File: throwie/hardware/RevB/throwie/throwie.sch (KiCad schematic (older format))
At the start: 24 parts, among them J1 CONN, Q1 2SC3356, Q2 SS8050-G, T1 TestPoints, T2 TestPoints, T3 TestPoints, T4 TestPoints, U1 C8051F850-A-GU, U2 MIC5231-3.3YM5-TR, X1 RO3101

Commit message: more layout
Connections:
- net 0.471: now also U1.2 (P0.2); no longer U1.14 (P1.4)
- net GNDREF: now also X1.3
- net at C4.2, Q1.1, Q2.3: no longer X1.3
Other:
- moved on the sheet: C4, Q2, R1
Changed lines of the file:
@@
 L throwie:RES_0603 R1
 U 1 1 6159CB9B
-P 5900 4650
-F 0 "R1" H 6075 4460 50  0000 C CNN
-F 1 "RES_0603" V 6075 4738 50  0001 L CNN
-F 2 "throwie:0603" H 5900 4650 50  0001 C CNN
-F 3 "" H 5900 4650 50  0001 C CNN
-F 4 "18K" H 6075 4551 50  0000 C CNN "Resistance"
-	1    5900 4650
+P 5950 4850
+F 0 "R1" H 6125 4660 50  0000 C CNN
+F 1 "RES_0603" V 6125 4938 50  0001 L CNN
+F 2 "throwie:0603" H 5950 4850 50  0001 C CNN
+F 3 "" H 5950 4850 50  0001 C CNN
+F 4 "18K" H 6125 4751 50  0000 C CNN "Resistance"
+	1    5950 4850
 	-1   0    0    1
 $EndComp
@@
 L power:GNDREF #PWR0111
 U 1 1 6159EFA4
-P 6250 4950
-F 0 "#PWR0111" H 6250 4700 50  0001 C CNN
-F 1 "GNDREF" H 6255 4777 50  0000 C CNN
-F 2 "" H 6250 4950 50  0001 C CNN
-F 3 "" H 6250 4950 50  0001 C CNN
-	1    6250 4950
+P 6250 5100
+F 0 "#PWR0111" H 6250 4850 50  0001 C CNN
+F 1 "GNDREF" H 6255 4927 50  0000 C CNN
+F 2 "" H 6250 5100 50  0001 C CNN
+F 3 "" H 6250 5100 50  0001 C CNN
+	1    6250 5100
 	1    0    0    -1
 $EndComp
@@
 L throwie:SS8050-G Q2
 U 1 1 615A6F3E
-P 6150 4650
-F 0 "Q2" H 6294 4696 50  0000 L CNN
-F 1 "SS8050-G" H 6294 4605 50  0000 L CNN
-F 2 "throwie:SS8050-G" H 6150 4650 50  0001 C CNN
-F 3 "" H 6150 4650 50  0001 C CNN
-	1    6150 4650
+P 6150 4850
+F 0 "Q2" H 6294 4896 50  0000 L CNN
+F 1 "SS8050-G" H 6294 4805 50  0000 L CNN
+F 2 "throwie:SS8050-G" H 6150 4850 50  0001 C CNN
+F 3 "" H 6150 4850 50  0001 C CNN
+	1    6150 4850
 	1    0    0    -1
 $EndComp
@@
 L throwie:CAP_0603 C4
 U 1 1 615A7727
-P 7000 4050
-F 0 "C4" H 7098 3971 50  0000 L CNN
-F 1 "CAP_0603" H 7098 3925 50  0001 L CNN
-F 2 "throwie:0603" H 7000 4050 50  0001 C CNN
-F 3 "" H 7000 4050 50  0001 C CNN
-F 4 "15pF" H 7098 3880 50  0000 L CNN "Capacitance"
-	1    7000 4050
+P 7100 4300
+F 0 "C4" H 7198 4221 50  0000 L CNN
+F 1 "CAP_0603" H 7198 4175 50  0001 L CNN
+F 2 "throwie:0603" H 7100 4300 50  0001 C CNN
+F 3 "" H 7100 4300 50  0001 C CNN
+F 4 "15pF" H 7198 4130 50  0000 L CNN "Capacitance"
+	1    7100 4300
 	1    0    0    -1
 $EndComp
@@
 $EndComp
 $Comp
-L throwie:RO3101 X1
-U 1 1 615AFB47
-P 6800 3950
-F 0 "X1" H 6800 4175 50  0000 C CNN
-F 1 "RO3101" H 6800 4084 50  0000 C CNN
-F 2 "throwie:R03101" H 6800 3950 50  0001 C CNN
-F 3 "" H 6800 3950 50  0001 C CNN
-	1    6800 3950
-	1    0    0    -1
-$EndComp
-$Comp
 L throwie:433MHz A1
 U 1 1 615B7977
@@
 	6600 3150 6600 3050
 Wire Wire Line
-	6250 4150 6250 4350
-Wire Wire Line
-	6250 4350 6800 4350
-Wire Wire Line
-	7000 4350 7000 4300
-Connection ~ 6250 4350
-Wire Wire Line
-	6250 4350 6250 4450
-Wire Wire Line
-	6800 4100 6800 4350
-Connection ~ 6800 4350
-Wire Wire Line
-	6800 4350 7000 4350
-Wire Wire Line
 	6650 3950 6600 3950
 Connection ~ 6600 3950
 Wire Wire Line
-	6950 3950 7000 3950
-Wire Wire Line
-	7000 3950 7000 4050
-Wire Wire Line
-	7000 3950 7000 3050
-Wire Wire Line
 	6250 3050 6600 3050
-Connection ~ 7000 3950
 Connection ~ 6600 3050
-Wire Wire Line
-	6600 3050 7000 3050
-Wire Wire Line
-	5550 4650 5200 4650
 Text Label 1200 3800 0    50   ~ 0
 MOD
-Text Label 1200 4400 0    50   ~ 0
+Text Label 1250 3300 0    50   ~ 0
 0.471
-Text Label 5200 4650 0    50   ~ 0
+Text Label 5200 4850 0    50   ~ 0
 MOD
 Wire Wire Line
@@
 	1050 1800 1050 1750
 Wire Wire Line
-	5900 4650 6050 4650
-Wire Wire Line
-	6250 4950 6250 4850
-Wire Wire Line
-	1800 4400 1200 4400
-NoConn ~ 1800 3300
-Wire Wire Line
 	1800 3800 1200 3800
-NoConn ~ 1800 3400
 $Comp
 L throwie:CAP_0603 C6
@@
 Wire Wire Line
 	5550 1400 5550 1350
+$Comp
+L throwie:RO3101 X1
+U 1 1 615AFB47
+P 6800 3950
+F 0 "X1" H 6800 4175 50  0000 C CNN
+F 1 "RO3101" H 6800 4084 50  0000 C CNN
+F 2 "throwie:R03101" H 6800 3950 50  0001 C CNN
+F 3 "" H 6800 3950 50  0001 C CNN
+	1    6800 3950
+	1    0    0    -1
+$EndComp
+$Comp
+L power:GNDREF #PWR?
+U 1 1 61988F00
+P 6800 4200
+F 0 "#PWR?" H 6800 3950 50  0001 C CNN
+F 1 "GNDREF" H 6805 4027 50  0000 C CNN
+F 2 "" H 6800 4200 50  0001 C CNN
+F 3 "" H 6800 4200 50  0001 C CNN
+	1    6800 4200
+	1    0    0    -1
+$EndComp
+Wire Wire Line
+	5600 4850 5200 4850
+Wire Wire Line
+	6050 4850 5950 4850
+Wire Wire Line
+	6250 5100 6250 5050
+Wire Wire Line
+	6250 4150 6250 4600
+Wire Wire Line
+	7100 4550 7100 4600
+Wire Wire Line
+	7100 4600 6250 4600
+Connection ~ 6250 4600
+Wire Wire Line
+	6250 4600 6250 4650
+Wire Wire Line
+	6800 4200 6800 4100
+Wire Wire Line
+	7100 4300 7100 3950
+Wire Wire Line
+	6950 3950 7100 3950
+Wire Wire Line
+	7100 3050 7100 3950
+Wire Wire Line
+	6600 3050 7100 3050
+Connection ~ 7100 3950
+NoConn ~ 1800 3400
+Wire Wire Line
+	1800 3300 1250 3300
+NoConn ~ 1800 4400
 $EndSCHEMATC

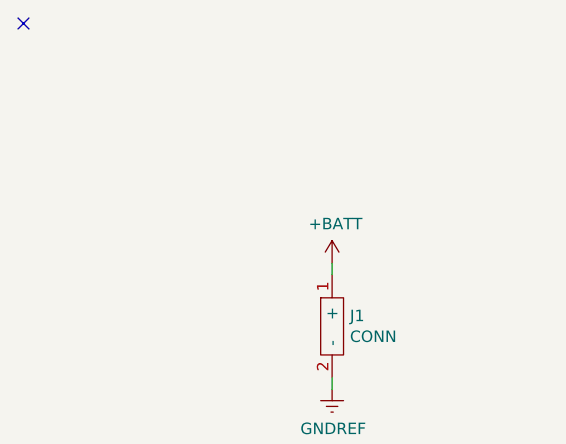
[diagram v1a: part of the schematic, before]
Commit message: more silk
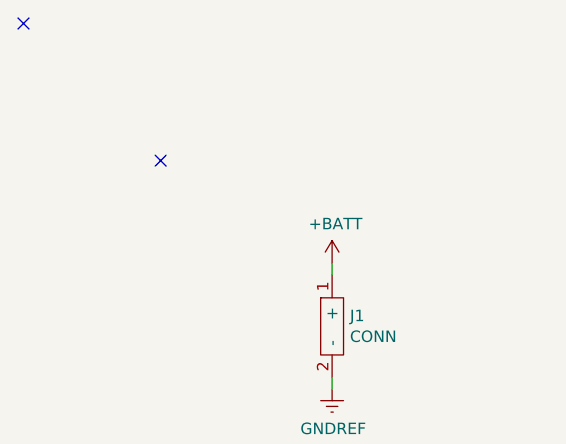
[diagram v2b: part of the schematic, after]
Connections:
- no-connect marks 18 -> 19
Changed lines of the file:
@@
 $EndComp
 $Comp
-L power:GNDREF #PWR?
+L power:GNDREF #PWR0116
 U 1 1 61988F00
 P 6800 4200
-F 0 "#PWR?" H 6800 3950 50  0001 C CNN
+F 0 "#PWR0116" H 6800 3950 50  0001 C CNN
 F 1 "GNDREF" H 6805 4027 50  0000 C CNN
 F 2 "" H 6800 4200 50  0001 C CNN
@@
 	1800 3300 1250 3300
 NoConn ~ 1800 4400
+NoConn ~ 300  800
 $EndSCHEMATC
